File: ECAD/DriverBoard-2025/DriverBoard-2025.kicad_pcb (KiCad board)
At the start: 2 copper layers, 56 x 45 mm, 18 parts, among them J1 XT30, J2 Conn_01x04, J3 Conn_01x04, J4 Conn_01x04, U1 TMC2209_SILENTSTEPSTICK, U2 TMC2209_SILENTSTEPSTICK, U3 TMC2209_SILENTSTEPSTICK

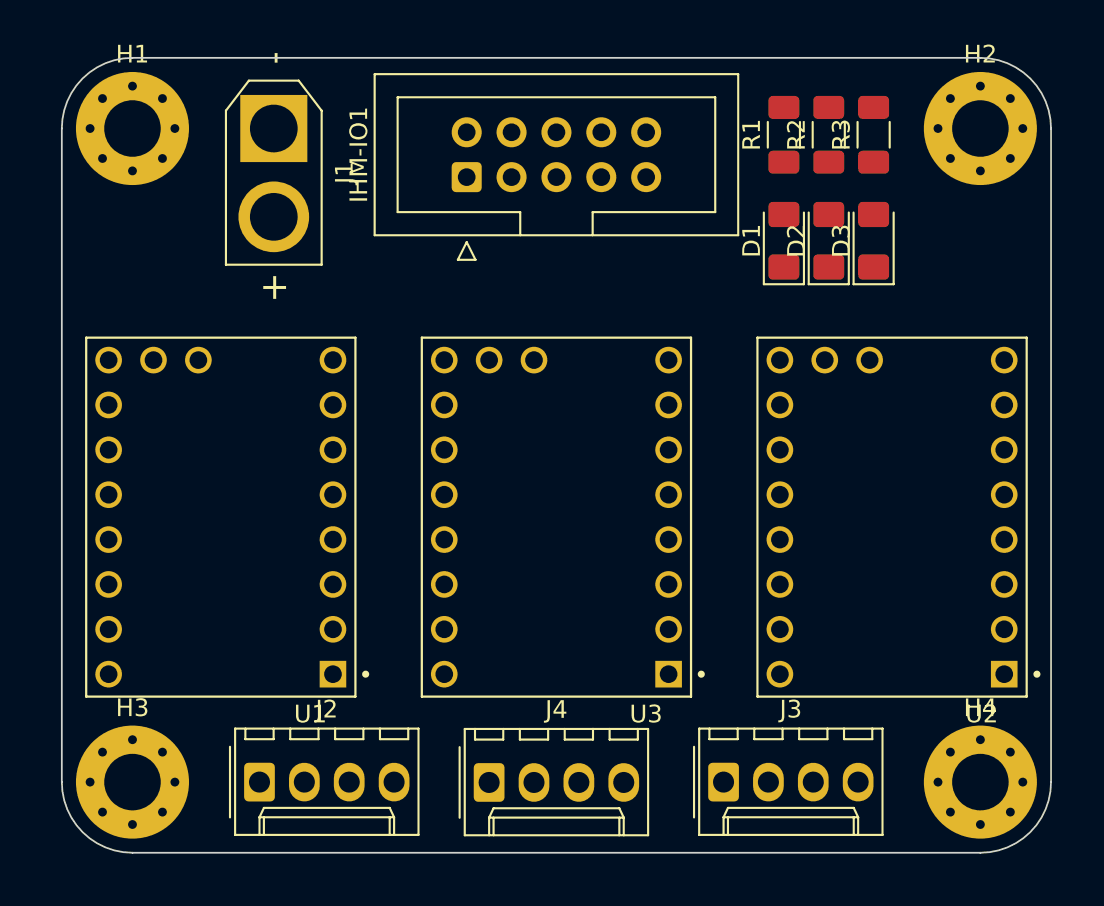
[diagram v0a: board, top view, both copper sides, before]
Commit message: Ad microstepping and capacitors
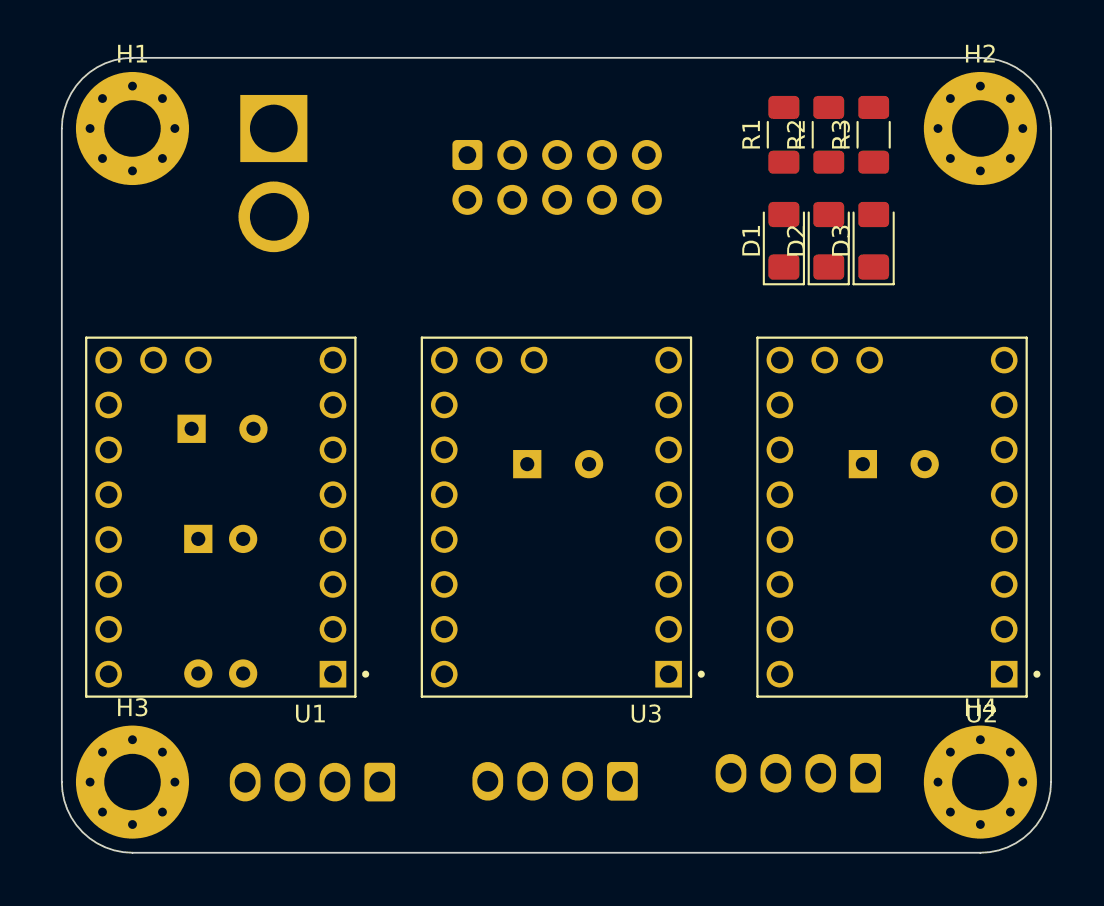
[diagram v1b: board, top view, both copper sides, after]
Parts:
- added C1: 100uF, Capacitor_THT:CP_Radial_D8.0mm_P3.50mm, B.Cu at (117.3, 71.0)
- added C2: 100uF, Capacitor_THT:CP_Radial_D8.0mm_P3.50mm, B.Cu at (136.3, 73.0)
- added C3: 100uF, Capacitor_THT:CP_Radial_D8.0mm_P3.50mm, B.Cu at (155.3, 73.0)
- added SW1: SW_DIP_x02, Button_Switch_THT:SW_DIP_SPSTx02_Slide_9.78x7.26mm_W7.62mm_P2.54mm, B.Cu at (117.7, 77.2)
- IHM-IO1, J1, J2, J3, J4: moved to B.Cu
- moved J3 8.06 mm to (155.5, 90.5), turned to 180 degrees
- moved J4 7.54 mm to (141.7, 91.0), turned to 180 degrees
- moved J2 6.81 mm to (128.0, 91.0), turned to 180 degrees
- moved IHM-IO1 1.25 mm to (133.0, 55.5), turned to -90 degrees
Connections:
- U1 pad 14: unconnected-(U1-MS2-Pad14) -> MS2
- U1 pad 15: unconnected-(U1-MS1-Pad15) -> MS1
- U2 pad 14: unconnected-(U2-MS2-Pad14) -> MS2
- U2 pad 15: unconnected-(U2-MS1-Pad15) -> MS1
- U3 pad 14: unconnected-(U3-MS2-Pad14) -> MS2
- U3 pad 15: unconnected-(U3-MS1-Pad15) -> MS1

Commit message: Premier routage
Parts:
- added J5: Fan, Connector_Molex:Molex_KK-254_AE-6410-02A_1x02_P2.54mm_Vertical, B.Cu at (116.5, 61.5)
- moved J3 8.32 mm to (147.2, 91.0), turned to 0 degrees
- moved J4 7.54 mm to (134.2, 91.0), turned to 0 degrees
- moved J2 6.81 mm to (121.2, 91.0), turned to 0 degrees
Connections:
- U1 pad 3: Net-(J2-Pin_2) -> Net-(J2-Pin_4)
- U1 pad 4: Net-(J2-Pin_4) -> Net-(J2-Pin_3)
- U1 pad 5: Net-(J2-Pin_3) -> Net-(J2-Pin_2)
- U2 pad 3: Net-(J3-Pin_2) -> Net-(J3-Pin_4)
- U2 pad 4: Net-(J3-Pin_4) -> Net-(J3-Pin_3)
- U2 pad 5: Net-(J3-Pin_3) -> Net-(J3-Pin_2)
- U3 pad 3: Net-(J4-Pin_2) -> Net-(J4-Pin_4)
- U3 pad 4: Net-(J4-Pin_4) -> Net-(J4-Pin_3)
- U3 pad 5: Net-(J4-Pin_3) -> Net-(J4-Pin_2)
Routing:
- net +24V: track 0.00 -> 112.0 mm, vias 0 -> 1
- net +3V3: track 0.00 -> 110.7 mm
- net +5V: track 0.00 -> 54.7 mm, vias 0 -> 2
- net EN: track 0.00 -> 54.5 mm
- net MS1: track 0.00 -> 49.9 mm, vias 0 -> 1
- net MS2: track 0.00 -> 47.0 mm, vias 0 -> 1
- net STEP_1: track 0.00 -> 43.3 mm
- net DIR_1: track 0.00 -> 39.9 mm
- net DIR_2: track 0.00 -> 35.9 mm
- net DIR_3: track 0.00 -> 34.2 mm, vias 0 -> 1
- net STEP_3: track 0.00 -> 31.9 mm, vias 0 -> 1
- net STEP_2: track 0.00 -> 31.4 mm
- net Net-(J3-Pin_1): track 0.00 -> 26.2 mm
- net Net-(J4-Pin_1): track 0.00 -> 23.0 mm
- net Net-(J3-Pin_2): track 0.00 -> 22.9 mm
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- added copper zone on B.Cu, net GND
- added copper zone on F.Cu, net GND

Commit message: PCB routing completed
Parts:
- SW1: footprint Button_Switch_THT:SW_DIP_SPSTx02_Slide_9.78x7.26mm_W7.62mm_P2.54mm -> Connector_PinHeader_2.54mm:PinHeader_2x02_P2.54mm_Vertical
- moved C2 5.23 mm to (137.7, 67.9), turned to -90 degrees
- moved C3 5.18 mm to (156.5, 67.9), turned to -90 degrees
- moved D1 5.12 mm to (156.0, 59.7)
- moved D3 5.12 mm to (150.9, 59.7)
- moved R1 5.09 mm to (156.0, 54.6)
- moved R3 5.09 mm to (150.9, 54.6)
- moved C1 3.22 mm to (118.4, 67.9), turned to -90 degrees
- moved SW1 1.15 mm to (118.9, 77.2), turned to 180 degrees
- moved J1 0.68 mm to (122.7, 54.0)
- moved D2 0.67 mm to (153.4, 59.7)
- moved R2 0.25 mm to (153.4, 54.6)
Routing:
- net EN: track 54.5 -> 78.0 mm, vias 0 -> 2
- net +3V3: track 110.7 -> 129.8 mm, vias 0 -> 2
- net +24V: track 112.0 -> 102.6 mm
- net MS2: track 47.0 -> 51.4 mm, vias 1 -> 0
- net Net-(J2-Pin_3): track 15.0 -> 17.3 mm
- net DIR_1: track 39.9 -> 42.1 mm
- net STEP_3: track 31.9 -> 30.0 mm, vias 1 -> 0
- net Net-(J3-Pin_1): track 26.2 -> 27.8 mm
- net Net-(J2-Pin_4): track 12.6 -> 13.9 mm
- net STEP_1: track 43.3 -> 44.3 mm
- net Net-(J2-Pin_1): track 20.5 -> 21.5 mm
- net Net-(J3-Pin_4): track 14.7 -> 15.6 mm
- net Net-(D2-A): track 2.96 -> 2.04 mm
- net Net-(D1-A): track 2.96 -> 2.04 mm
- net Net-(D3-A): track 2.96 -> 2.04 mm
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
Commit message: update silkscreen
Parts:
- added kibuzzard-675DF2CA: G***, kibuzzard-675DF2CA, F.Cu at (133.0, 60.5)
- added kibuzzard-675DF2CA: G***, kibuzzard-675DF2CA, F.Cu at (153.4, 63.2)
- added kibuzzard-675DF2CA: G***, kibuzzard-675DF2CA, F.Cu at (118.9, 61.5)
- added kibuzzard-675DF3A9: G***, kibuzzard-675DF3A9, F.Cu at (150.9, 64.0)
- added kibuzzard-675DF3A9: G***, kibuzzard-675DF3A9, F.Cu at (143.1, 61.1)
- added kibuzzard-675DF3AF: G***, kibuzzard-675DF3AF, F.Cu at (126.5, 58.9)
- added kibuzzard-675DF3AF: G***, kibuzzard-675DF3AF, F.Cu at (155.9, 63.6)
- added kibuzzard-675DF3F9: G***, kibuzzard-675DF3F9, F.Cu at (125.0, 88.6)
- added kibuzzard-675DF3F9: G***, kibuzzard-675DF3F9, B.Cu at (125.0, 87.1)
- added kibuzzard-675DF4D6: G***, kibuzzard-675DF4D6, F.Cu at (138.1, 53.1)
- added kibuzzard-675DF53C: G***, kibuzzard-675DF53C, F.Cu at (140.6, 52.5)
- added kibuzzard-675DF53C: G***, kibuzzard-675DF53C, F.Cu at (132.9, 52.4)
- added kibuzzard-675DF579: G***, kibuzzard-675DF579, F.Cu at (140.6, 61.1)
- added kibuzzard-675DF582: G***, kibuzzard-675DF582, F.Cu at (137.9, 88.6)
- added kibuzzard-675DF582: G***, kibuzzard-675DF582, B.Cu at (138.2, 87.1)
- added kibuzzard-675DF588: G***, kibuzzard-675DF588, F.Cu at (151.1, 88.6)
- added kibuzzard-675DF588: G***, kibuzzard-675DF588, B.Cu at (150.9, 87.1)
- added kibuzzard-675DF59D: G***, kibuzzard-675DF59D, F.Cu at (143.2, 52.5)
- added kibuzzard-675DF5B3: G***, kibuzzard-675DF5B3, F.Cu at (135.5, 52.4)
- added kibuzzard-675DF5B8: G***, kibuzzard-675DF5B8, F.Cu at (135.4, 61.1)
- added kibuzzard-675DF6AB: G***, kibuzzard-675DF6AB, B.Cu at (119.4, 63.0)
- added kibuzzard-675DF6AB: G***, kibuzzard-675DF6AB, B.Cu at (121.4, 79.8)
- added kibuzzard-675DF6F1: G***, kibuzzard-675DF6F1, B.Cu at (116.3, 75.2)
- added kibuzzard-675DF6F8: G***, kibuzzard-675DF6F8, B.Cu at (118.9, 75.2)
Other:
- board text added: "Karibous 2025"
